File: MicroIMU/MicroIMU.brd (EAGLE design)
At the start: 8.1 x 8.8 mm, 17 parts

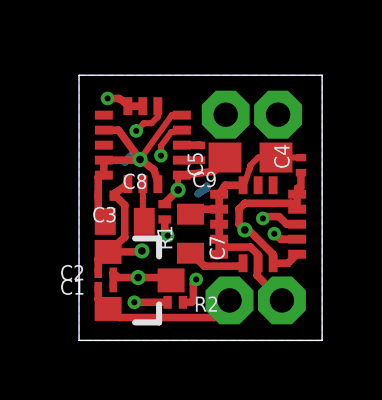
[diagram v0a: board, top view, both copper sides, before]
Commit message: Rotated L3GD20H so that X and Y axes of the two chips are aligned
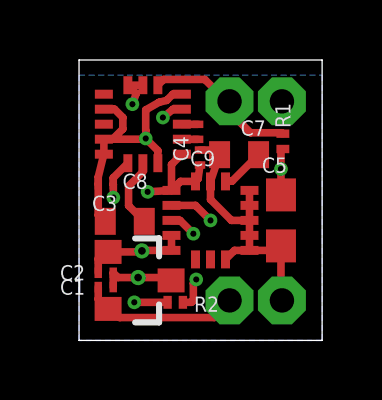
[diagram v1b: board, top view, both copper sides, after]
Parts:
- moved R1 4.58 mm to (6.79, 6.64), turned to 270 degrees
- moved C4 3.38 mm to (4.03, 6.10)
- moved C7 3.09 mm to (5.33, 6.19), turned to 180 degrees
- moved C5 2.33 mm to (6.73, 4.00), turned to 270 degrees
- moved U$1 1.59 mm to (4.38, 4.00), turned to 0 degrees
- moved C9 0.70 mm to (3.97, 6.95)
- moved U$3 0.70 mm to (2.13, 7.21)
- moved SCL 0.46 mm to (6.76, 7.97)
- moved SDA 0.46 mm to (5.02, 7.97)
- moved C3 0.38 mm to (0.89, 5.21)
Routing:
- net SDA: track 15.4 -> 11.0 mm, vias 3 -> 1
- net +3V3: track 17.3 -> 13.7 mm, vias 5 -> 6
- net SCL: track 15.2 -> 17.0 mm
- net N$1: track 1.27 -> 2.35 mm
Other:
- board size 8.1 x 8.8 mm -> 8.1 x 9.3 mm
